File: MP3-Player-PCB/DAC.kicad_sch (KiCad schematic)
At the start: 16 parts, among them U401 TAD5242, U402 TPD4E1U06, U403 ST-0322D00-071-1A2H

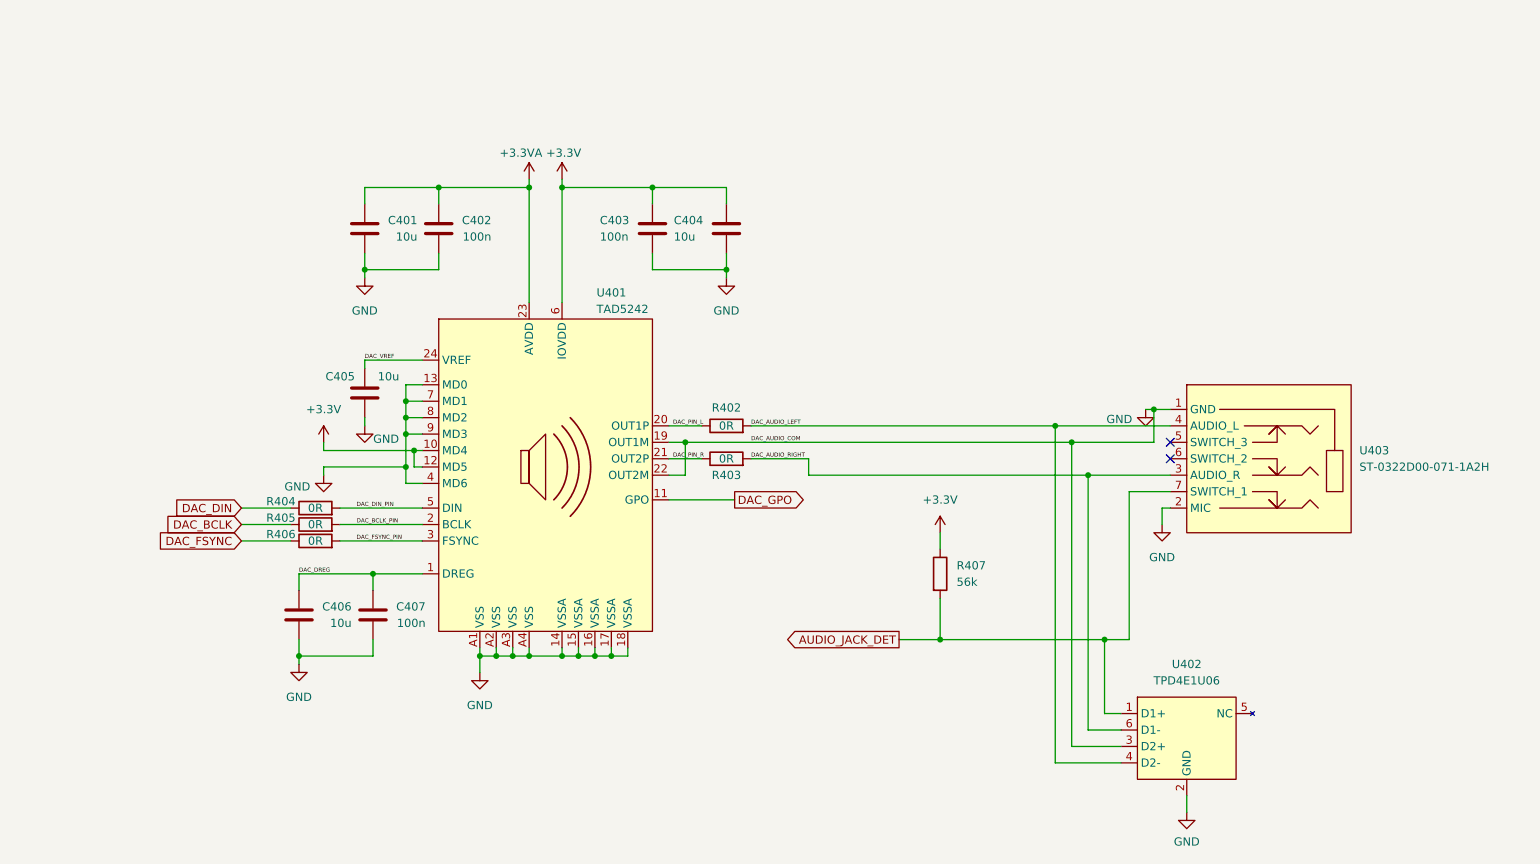
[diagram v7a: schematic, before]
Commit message: Fixed all ERC errors
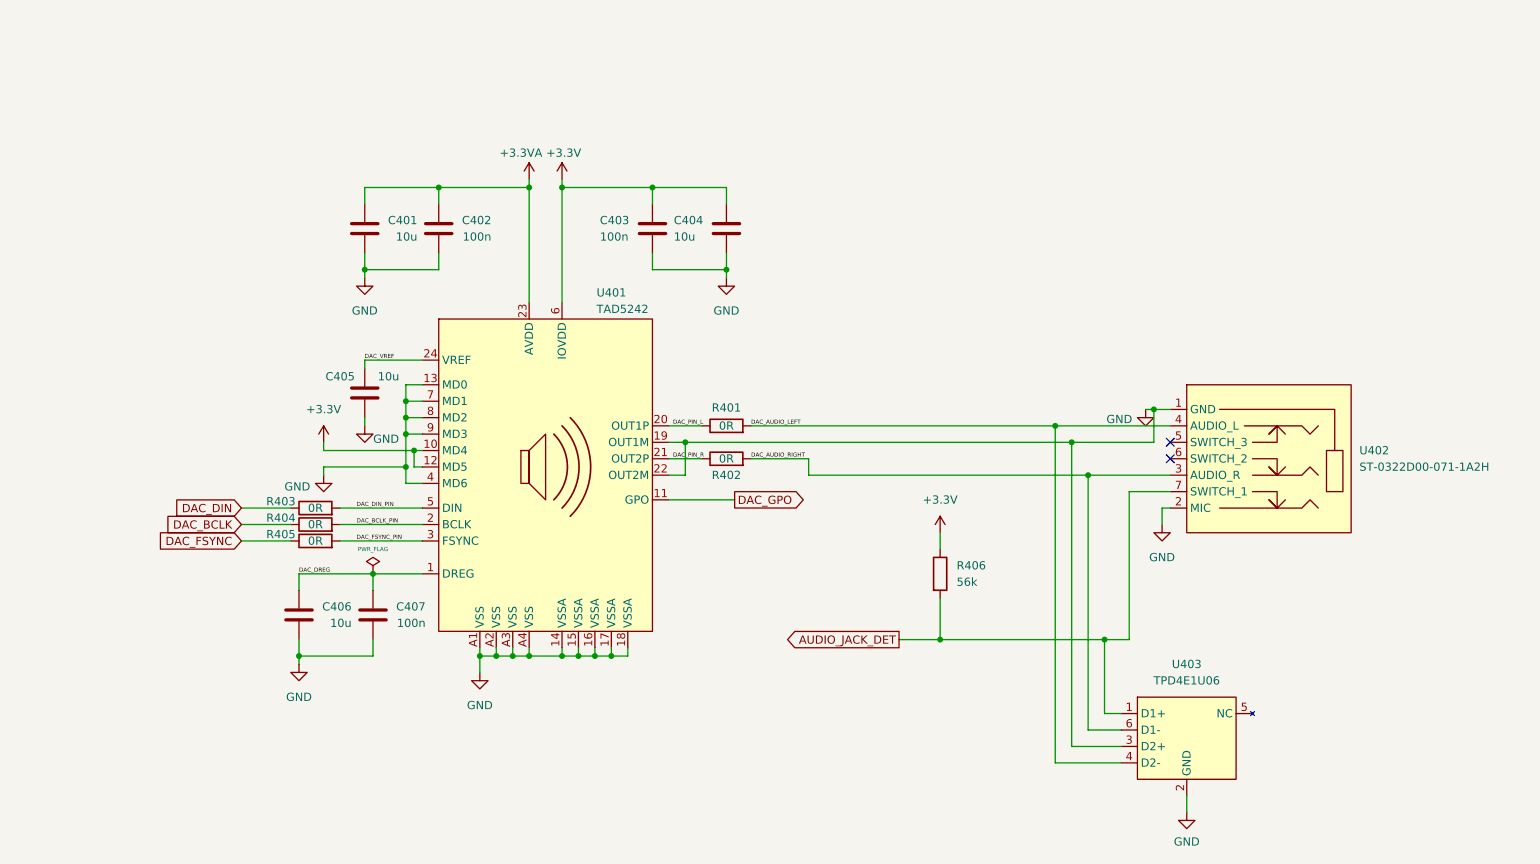
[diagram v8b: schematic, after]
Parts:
- renumbered R402 to R401, R403 to R402, R404 to R403, R405 to R404, R406 to R405, R407 to R406, U403 to U402, U402 to U403
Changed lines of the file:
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@@
-		)
-	)
-	(label "DAC_AUDIO_COM"
-		(at 143.51 95.25 0)
-		(effects
-			(font
-				(size 0.635 0.635)
-			)
-			(justify left bottom)
 		)
 	)
@@
 		(dnp no)
 		(fields_autoplaced yes)
-		(property "Reference" "U402"
+		(property "Reference" "U403"
 			(at 210.82 129.54 0)
 			(effects
@@
 			(project "MP3-Player"
 				(path "/3f51ea9b-d2e1-4711-a47c-269e1b97e0f4/55939feb-9632-43ca-a0aa-b7cf8cf1876d"
-					(reference "U402")
+					(reference "U403")
 					(unit 1)
 				)
@@
 		(dnp no)
 		(fields_autoplaced yes)
-		(property "Reference" "U403"
+		(property "Reference" "U402"
 			(at 237.49 96.5199 0)
 			(effects
@@
 			(project ""
 				(path "/3f51ea9b-d2e1-4711-a47c-269e1b97e0f4/55939feb-9632-43ca-a0aa-b7cf8cf1876d"
-					(reference "U403")
+					(reference "U402")
+					(unit 1)
+				)
+			)
+		)
+	)
+	(symbol
+		(lib_id "power:PWR_FLAG")
+		(at 85.09 115.57 0)
+		(unit 1)
+		(exclude_from_sim no)
+		(in_bom yes)
+		(on_board yes)
+		(dnp no)
+		(fields_autoplaced yes)
+		(property "Reference" "#FLG0401"
+			(at 85.09 113.665 0)
+			(effects
+				(font
+					(size 1.27 1.27)
+				)
+				(hide yes)
+			)
+		)
+		(property "Value" "PWR_FLAG"
+			(at 85.09 111.76 0)
+			(effects
+				(font
+					(size 0.635 0.635)
+				)
+			)
+		)
+		(property "Footprint" ""
+			(at 85.09 115.57 0)
+			(effects
+				(font
+					(size 1.27 1.27)
+				)
+				(hide yes)
+			)
+		)
+		(property "Datasheet" "~"
+			(at 85.09 115.57 0)
+			(effects
+				(font
+					(size 1.27 1.27)
+				)
+				(hide yes)
+			)
+		)
+		(property "Description" "Special symbol for telling ERC where power comes from"
+			(at 85.09 115.57 0)
+			(effects
+				(font
+					(size 1.27 1.27)
+				)
+				(hide yes)
+			)
+		)
+		(pin "1"
+		)
+		(instances
+			(project ""
+				(path "/3f51ea9b-d2e1-4711-a47c-269e1b97e0f4/55939feb-9632-43ca-a0aa-b7cf8cf1876d"
+					(reference "#FLG0401")
 					(unit 1)
 				)
@@
 		(dnp no)
 		(fields_autoplaced yes)
-		(property "Reference" "#PWR0413"
+		(property "Reference" "#PWR0409"
 			(at 207.01 114.3 0)
 			(effects
@@
 			(project ""
 				(path "/3f51ea9b-d2e1-4711-a47c-269e1b97e0f4/55939feb-9632-43ca-a0aa-b7cf8cf1876d"
-					(reference "#PWR0413")
+					(reference "#PWR0409")
 					(unit 1)
 				)
@@
 		(dnp no)
 		(fields_autoplaced yes)
-		(property "Reference" "#PWR0411"
+		(property "Reference" "#PWR0412"
 			(at 101.6 137.16 0)
 			(effects
@@
 			(project "MP3-Player"
 				(path "/3f51ea9b-d2e1-4711-a47c-269e1b97e0f4/55939feb-9632-43ca-a0aa-b7cf8cf1876d"
-					(reference "#PWR0411")
+					(reference "#PWR0412")
 					(unit 1)
 				)
@@
 		(on_board yes)
 		(dnp no)
-		(property "Reference" "R406"
+		(property "Reference" "R405"
 			(at 70.866 109.474 90)
 			(effects
@@
 			(project "MP3-Player"
 				(path "/3f51ea9b-d2e1-4711-a47c-269e1b97e0f4/55939feb-9632-43ca-a0aa-b7cf8cf1876d"
-					(reference "R406")
+					(reference "R405")
 					(unit 1)
 				)
@@
 		(on_board yes)
 		(dnp no)
-		(property "Reference" "R402"
+		(property "Reference" "R401"
 			(at 139.7 89.916 90)
 			(effects
@@
 			(project "MP3-Player"
 				(path "/3f51ea9b-d2e1-4711-a47c-269e1b97e0f4/55939feb-9632-43ca-a0aa-b7cf8cf1876d"
-					(reference "R402")
+					(reference "R401")
 					(unit 1)
 				)
@@
 		(on_board yes)
 		(dnp no)
-		(property "Reference" "R403"
+		(property "Reference" "R402"
 			(at 139.7 100.33 90)
 			(effects
@@
 			(project "MP3-Player"
 				(path "/3f51ea9b-d2e1-4711-a47c-269e1b97e0f4/55939feb-9632-43ca-a0aa-b7cf8cf1876d"
-					(reference "R403")
+					(reference "R402")
 					(unit 1)
 				)
@@
 		(dnp no)
 		(fields_autoplaced yes)
-		(property "Reference" "#PWR0409"
+		(property "Reference" "#PWR0410"
 			(at 172.72 113.03 0)
 			(effects
@@
 			(project "MP3-Player"
 				(path "/3f51ea9b-d2e1-4711-a47c-269e1b97e0f4/55939feb-9632-43ca-a0aa-b7cf8cf1876d"
-					(reference "#PWR0409")
+					(reference "#PWR0410")
 					(unit 1)
 				)
@@
 		(on_board yes)
 		(dnp no)
-		(property "Reference" "#PWR0412"
+		(property "Reference" "#PWR0413"
 			(at 210.82 158.75 0)
 			(effects
@@
 			(project "MP3-Player"
 				(path "/3f51ea9b-d2e1-4711-a47c-269e1b97e0f4/55939feb-9632-43ca-a0aa-b7cf8cf1876d"
-					(reference "#PWR0412")
+					(reference "#PWR0413")
 					(unit 1)
 				)
@@
 		(on_board yes)
 		(dnp no)
-		(property "Reference" "R405"
+		(property "Reference" "R404"
 			(at 70.866 106.934 90)
 			(effects
@@
 			(project "MP3-Player"
 				(path "/3f51ea9b-d2e1-4711-a47c-269e1b97e0f4/55939feb-9632-43ca-a0aa-b7cf8cf1876d"
-					(reference "R405")
+					(reference "R404")
 					(unit 1)
 				)
@@
 		(dnp no)
 		(fields_autoplaced yes)
-		(property "Reference" "R407"
+		(property "Reference" "R406"
 			(at 175.26 114.2999 0)
 			(effects
@@
 			(project "MP3-Player"
 				(path "/3f51ea9b-d2e1-4711-a47c-269e1b97e0f4/55939feb-9632-43ca-a0aa-b7cf8cf1876d"
-					(reference "R407")
+					(reference "R406")
 					(unit 1)
 				)
@@
 		(dnp no)
 		(fields_autoplaced yes)
-		(property "Reference" "#PWR0410"
+		(property "Reference" "#PWR0411"
 			(at 73.66 135.89 0)
 			(effects
@@
 			(project "MP3-Player"
 				(path "/3f51ea9b-d2e1-4711-a47c-269e1b97e0f4/55939feb-9632-43ca-a0aa-b7cf8cf1876d"
-					(reference "#PWR0410")
+					(reference "#PWR0411")
 					(unit 1)
 				)
@@
 		(on_board yes)
 		(dnp no)
-		(property "Reference" "R404"
+		(property "Reference" "R403"
 			(at 70.866 104.394 90)
 			(effects
@@
 			(project ""
 				(path "/3f51ea9b-d2e1-4711-a47c-269e1b97e0f4/55939feb-9632-43ca-a0aa-b7cf8cf1876d"
-					(reference "R404")
-					(unit 1)
-				)
+					(reference "R403")
+					(unit 1)
+				)
